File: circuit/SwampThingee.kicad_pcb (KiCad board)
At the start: 2 copper layers, 100 x 60 mm, 87 parts, among them J1 CONN_01X04, J2 HOLE, J3 HOLE, J4 HOLE, J5 HOLE, Q1 IRFS52N15DTRLP, Q2 BC547, SW1 RESET, SW10 4S, SW3 HEAD/AD, SW9 6S, U1 TPS560430, U2 LM1117-5.0, U3 MAX6457, U4 LM1117-3.3, U5 TPA3220, U6 CSR_DebugSmall, U7 CSR8645_MODULE

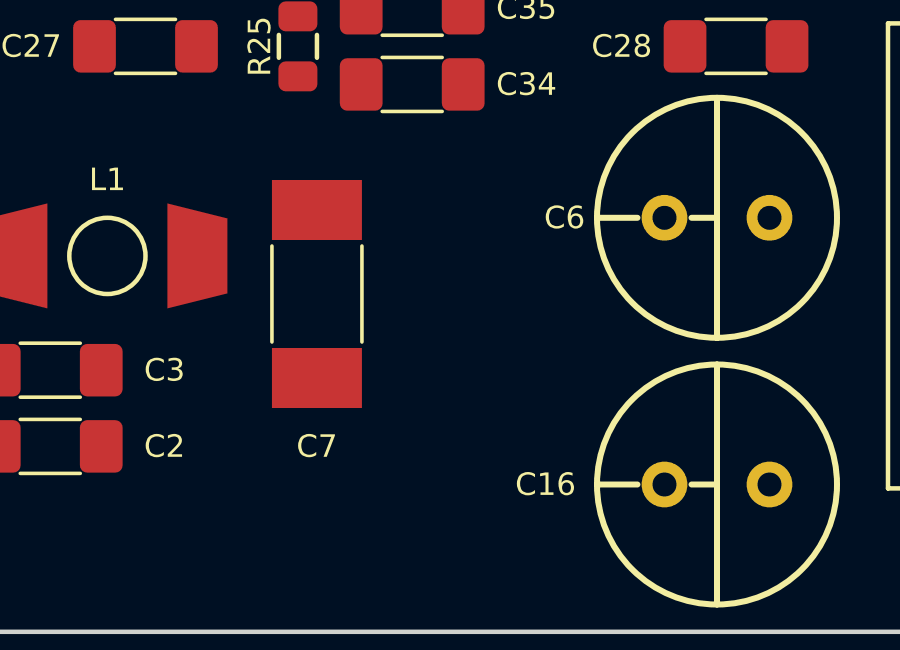
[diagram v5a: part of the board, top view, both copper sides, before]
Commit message: double the 1812 decouple caps
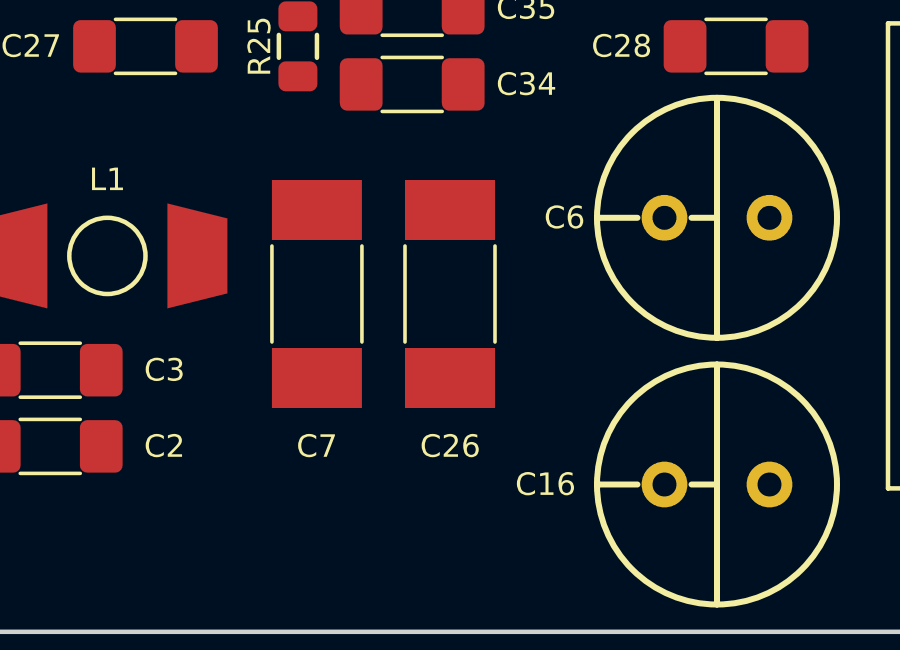
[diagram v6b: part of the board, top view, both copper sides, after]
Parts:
- added C26: 15μF, NovaBox:C_1812, F.Cu at (116.2, 78.7)
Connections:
- J2 pad 1: (no net) -> Net-(J2-Pad1)
- J3 pad 1: (no net) -> Net-(J3-Pad1)
- J4 pad 1: (no net) -> Net-(J4-Pad1)
- J5 pad 1: (no net) -> Net-(J5-Pad1)
- S1 pad 1: (no net) -> Net-(S1-Pad1)
- U5 pad 12: (no net) -> Net-(U5-Pad12)
- U5 pad 13: (no net) -> Net-(U5-Pad13)
- U7 pad 10: (no net) -> Net-(U7-Pad10)
- U7 pad 11: (no net) -> Net-(U7-Pad11)
- U7 pad 18: (no net) -> Net-(U7-Pad18)
- U7 pad 19: (no net) -> Net-(U7-Pad19)
- U7 pad 20: (no net) -> Net-(U7-Pad20)
- U7 pad 21: (no net) -> Net-(U7-Pad21)
- U7 pad 22: (no net) -> Net-(U7-Pad22)
- U7 pad 23: (no net) -> Net-(U7-Pad23)
- U7 pad 26: (no net) -> Net-(U7-Pad26)
- U7 pad 27: (no net) -> Net-(U7-Pad27)
- U7 pad 28: (no net) -> Net-(U7-Pad28)
- U7 pad 29: (no net) -> Net-(U7-Pad29)
- U7 pad 30: (no net) -> Net-(U7-Pad30)
- U7 pad 31: (no net) -> Net-(U7-Pad31)
- U7 pad 32: (no net) -> Net-(U7-Pad32)
- U7 pad 33: (no net) -> Net-(U7-Pad33)
- U7 pad 34: (no net) -> Net-(U7-Pad34)
- U7 pad 35: (no net) -> Net-(U7-Pad35)
- U7 pad 36: (no net) -> Net-(U7-Pad36)
- U7 pad 37: (no net) -> Net-(U7-Pad37)
- U7 pad 38: (no net) -> Net-(U7-Pad38)
- U7 pad 4: (no net) -> Net-(U7-Pad4)
- U7 pad 43: (no net) -> Net-(U7-Pad43)

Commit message: capacitors
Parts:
- C13, C14, C16, C20, C4, C6: value 330μF -> 470μF
- moved R7 0.64 mm to (112.4, 41.9)
- moved R5 0.63 mm to (112.4, 38.1)
- turned R6 to 0 degrees
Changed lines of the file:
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@@
   )
   (module NovaBox:R_0805 (layer F.Cu)
-    (at 112.395 38.735 90)
+    (at 112.395 38.1 90)
     (descr "Resistor SMD 0805, reflow soldering, Vishay (see dcrcw.pdf)")
     (tags "resistor 0805")
@@
   )
   (module NovaBox:R_0805 (layer F.Cu)
-    (at 112.395 42.545 270)
+    (at 112.395 41.91 270)
     (descr "Resistor SMD 0805, reflow soldering, Vishay (see dcrcw.pdf)")
     (tags "resistor 0805")
@@
       (effects (font (size 0.75 0.75) (thickness 0.15)))
     )
-    (fp_text value 330μF (at 1 -2 180) (layer F.Fab)
+    (fp_text value 470μF (at 1 -2 180) (layer F.Fab)
       (effects (font (size 0.127 0.127) (thickness 0.03175)))
     )
@@
       (effects (font (size 0.75 0.75) (thickness 0.15)))
     )
-    (fp_text value 330μF (at 1 -2 180) (layer F.Fab)
+    (fp_text value 470μF (at 1 -2 180) (layer F.Fab)
       (effects (font (size 0.127 0.127) (thickness 0.03175)))
     )
@@
       (effects (font (size 0.75 0.75) (thickness 0.15)))
     )
-    (fp_text value 330μF (at 1 -2 180) (layer F.Fab)
+    (fp_text value 470μF (at 1 -2 180) (layer F.Fab)
       (effects (font (size 0.127 0.127) (thickness 0.03175)))
     )
@@
       (effects (font (size 0.75 0.75) (thickness 0.15)))
     )
-    (fp_text value 330μF (at 1 -2) (layer F.Fab)
+    (fp_text value 470μF (at 1 -2) (layer F.Fab)
       (effects (font (size 0.127 0.127) (thickness 0.03175)))
     )
@@
       (effects (font (size 0.75 0.75) (thickness 0.15)))
     )
-    (fp_text value 330μF (at 1 -2 180) (layer F.Fab)
+    (fp_text value 470μF (at 1 -2 180) (layer F.Fab)
       (effects (font (size 0.127 0.127) (thickness 0.03175)))
     )
@@
       (effects (font (size 0.75 0.75) (thickness 0.15)))
     )
-    (fp_text value 330μF (at 1 -2) (layer F.Fab)
+    (fp_text value 470μF (at 1 -2) (layer F.Fab)
       (effects (font (size 0.127 0.127) (thickness 0.03175)))
     )
@@
   )
   (module NovaBox:R_0805 (layer F.Cu)
-    (at 83.185 82.55 180)
-    (descr "Resistor SMD 0805, reflow soldering, Vishay (see dcrcw.pdf)")
-    (tags "resistor 0805")
-    (attr smd)
-    (fp_text reference R6 (at 0 -1.27) (layer F.SilkS)
-      (effects (font (size 0.75 0.75) (thickness 0.15)))
-    )
-    (fp_text value 10K (at -0.635 0 270) (layer F.Fab) hide
-      (effects (font (size 0.0254 0.0254) (thickness 0.001)))
-    )
-    (fp_line (start -0.381 -0.635) (end 0.381 -0.635) (layer F.SilkS) (width 0.15))
-    (fp_line (start -0.381 0.635) (end 0.381 0.635) (layer F.SilkS) (width 0.15))
-    (pad 1 smd roundrect (at -1 0 180) (size 1 1.3) (layers F.Cu F.Paste F.Mask) (roundrect_rratio 0.25)
-      (net 2 +BATT))
-    (pad 2 smd roundrect (at 1 0 180) (size 1 1.3) (layers F.Cu F.Paste F.Mask) (roundrect_rratio 0.25)
+    (at 83.185 82.55)
+    (descr "Resistor SMD 0805, reflow soldering, Vishay (see dcrcw.pdf)")
+    (tags "resistor 0805")
+    (attr smd)
+    (fp_text reference R6 (at 0 1.27 -180) (layer F.SilkS)
+      (effects (font (size 0.75 0.75) (thickness 0.15)))
+    )
+    (fp_text value 10K (at -0.635 0 90) (layer F.Fab) hide
+      (effects (font (size 0.0254 0.0254) (thickness 0.001)))
+    )
+    (fp_line (start -0.381 -0.635) (end 0.381 -0.635) (layer F.SilkS) (width 0.15))
+    (fp_line (start -0.381 0.635) (end 0.381 0.635) (layer F.SilkS) (width 0.15))
+    (pad 1 smd roundrect (at -1 0) (size 1 1.3) (layers F.Cu F.Paste F.Mask) (roundrect_rratio 0.25)
+      (net 2 +BATT))
+    (pad 2 smd roundrect (at 1 0) (size 1 1.3) (layers F.Cu F.Paste F.Mask) (roundrect_rratio 0.25)
       (net 26 "Net-(D3-Pad2)"))
     (model Resistors_SMD.3dshapes/R_0805.wrl

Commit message: started routing swamp thingee
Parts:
- removed C14, C20: 470μF, NovaBox:CPOL_D8_P3.5
- moved C16 35.0 mm to (142.2, 54.6), turned to 0 degrees
- moved C4 31.0 mm to (133.3, 64.8)
- moved C13 27.1 mm to (142.2, 64.8), turned to 0 degrees
- moved C8 26.1 mm to (113.0, 76.2), turned to 0 degrees
- moved C6 23.1 mm to (133.3, 54.6)
- moved C7 5.43 mm to (109.9, 83.8)
- moved C26 5.42 mm to (114.3, 83.8)
- moved BT1 3.81 mm to (74.3, 85.7)
- moved D3 3.24 mm to (91.4, 83.2), turned to 180 degrees
- moved R29 2.69 mm to (81.3, 56.5)
- moved L3 2.54 mm to (137.8, 80.0)
- moved L2 2.54 mm to (137.8, 40.0)
- moved R2 2.01 mm to (92.7, 78.1)
- moved R5 2.01 mm to (113.0, 40.0)
- moved R7 2.01 mm to (113.0, 43.8)
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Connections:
- J2 pad 1: Net-(J2-Pad1) -> (no net)
- J3 pad 1: Net-(J3-Pad1) -> (no net)
- J4 pad 1: Net-(J4-Pad1) -> (no net)
- J5 pad 1: Net-(J5-Pad1) -> (no net)
- RN1 pad 6: /GRN -> /BLU
- RN1 pad 7: /GRN -> /BLU
- RN1 pad 8: /BLU -> /GRN
- S1 pad 1: Net-(S1-Pad1) -> /GAIN_SLV
- S1 pad 2: Net-(R5-Pad2) -> (no net)
- S1 pad 4: Net-(R7-Pad2) -> Net-(R5-Pad2)
- S1 pad 5: /GAIN_SLV -> Net-(R7-Pad2)
- U5 pad 12: Net-(U5-Pad12) -> (no net)
- U5 pad 13: Net-(U5-Pad13) -> (no net)
- U7 pad 10: Net-(U7-Pad10) -> (no net)
- U7 pad 11: Net-(U7-Pad11) -> (no net)
- U7 pad 18: Net-(U7-Pad18) -> (no net)
- U7 pad 19: Net-(U7-Pad19) -> (no net)
- U7 pad 20: Net-(U7-Pad20) -> (no net)
- U7 pad 21: Net-(U7-Pad21) -> (no net)
- U7 pad 22: Net-(U7-Pad22) -> (no net)
- U7 pad 23: Net-(U7-Pad23) -> (no net)
- U7 pad 26: Net-(U7-Pad26) -> (no net)
- U7 pad 27: Net-(U7-Pad27) -> (no net)
- U7 pad 28: Net-(U7-Pad28) -> (no net)
- U7 pad 29: Net-(U7-Pad29) -> (no net)
- U7 pad 30: Net-(U7-Pad30) -> (no net)
- U7 pad 31: Net-(U7-Pad31) -> (no net)
- U7 pad 32: Net-(U7-Pad32) -> (no net)
- U7 pad 33: Net-(U7-Pad33) -> (no net)
- U7 pad 34: Net-(U7-Pad34) -> (no net)
- U7 pad 35: Net-(U7-Pad35) -> (no net)
- U7 pad 36: Net-(U7-Pad36) -> (no net)
- U7 pad 37: Net-(U7-Pad37) -> (no net)
- U7 pad 38: Net-(U7-Pad38) -> (no net)
- U7 pad 4: Net-(U7-Pad4) -> (no net)
- U7 pad 43: Net-(U7-Pad43) -> (no net)
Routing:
- net +BATT: track 0.00 -> 148.7 mm, vias 0 -> 6
- net +5V: track 0.00 -> 92.6 mm
- net SPK_RP: track 0.00 -> 59.6 mm
- net SPK_RN: track 0.00 -> 59.0 mm
- net SPK_LP: track 0.00 -> 56.4 mm
- net SPK_LN: track 0.00 -> 55.7 mm
- net +3V3: track 0.00 -> 47.2 mm
- net /OUT1_P: track 0.00 -> 31.9 mm
- net /OUT2_M: track 0.00 -> 29.8 mm
- net /OUT1_M: track 0.00 -> 26.3 mm
- net +7.5V: track 0.00 -> 24.2 mm
- net /OUT2_P: track 0.00 -> 22.5 mm
- net /SPI_PCM: track 0.00 -> 21.5 mm
- net VBUS: track 0.00 -> 18.6 mm, vias 0 -> 1
- net HEAD: track 0.00 -> 17.7 mm, vias 0 -> 1
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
